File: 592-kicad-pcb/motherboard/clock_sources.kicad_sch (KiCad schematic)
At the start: 28 parts, among them J6 U.FL, U5 SMXS-04K, U6 SX3M10.000B10F20TNN, U7 74LVC1T45GW, U8 SN74LVC1G3157DBVR, U9 SN74LVC1G3157DBVR, Y1 NX3225GA-25.000M-STD-CRG-2, Y2 Si5351A

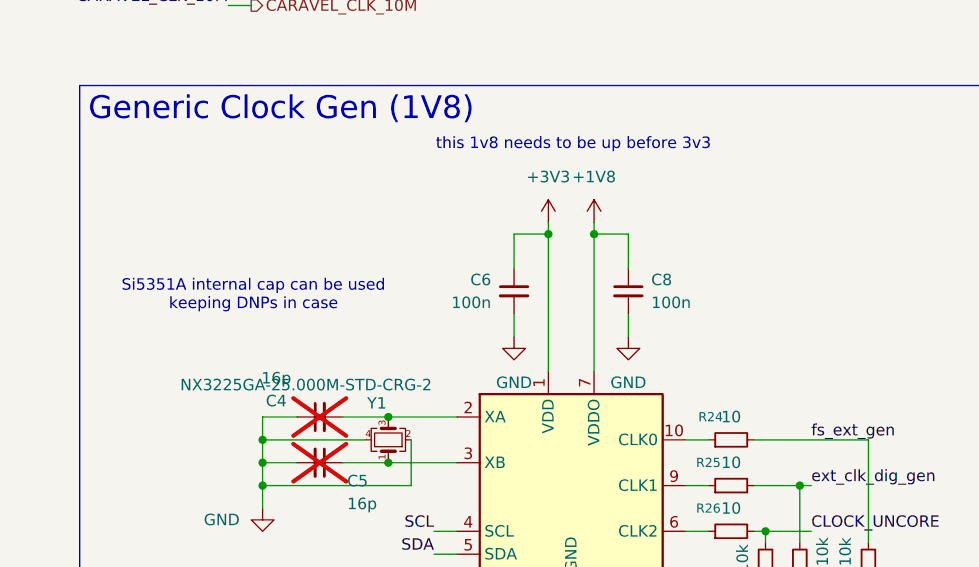
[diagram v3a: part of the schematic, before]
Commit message: add JLC part num for parts, footprints
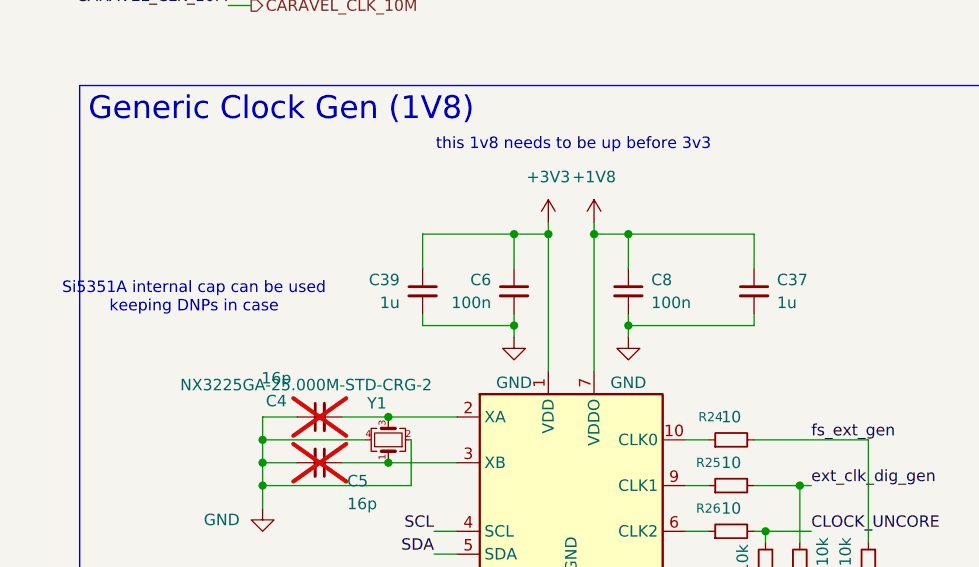
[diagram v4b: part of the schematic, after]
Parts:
- added C37, C39: 1u, Capacitor_SMD:C_0603_1608Metric, symbol Device:C_Small
- C10, C6, C7, C8, C9: footprint Capacitor_SMD:C_0603_1608Metric -> Capacitor_SMD:C_0402_1005Metric; LCSC (none) -> C1525
- C11: footprint Capacitor_SMD:C_0603_1608Metric -> Capacitor_SMD:C_0402_1005Metric; LCSC (none) -> C15195
- C4, C5: footprint Capacitor_SMD:C_0603_1608Metric -> Capacitor_SMD:C_0402_1005Metric
- J6: LCSC (none) -> C5137195
- R22, R23, R27, R28, R29, R30, R31, R32, R33: footprint Resistor_SMD:R_0603_1608Metric -> Resistor_SMD:R_0402_1005Metric; LCSC (none) -> C25744
- R24, R25, R26: footprint Resistor_SMD:R_0603_1608Metric -> Resistor_SMD:R_0402_1005Metric; LCSC (none) -> C25077
- U5: LCSC (none) -> C5439763
- U6: footprint (none) -> Crystal:Crystal_SMD_3225-4Pin_3.2x2.5mm; LCSC (none) -> C5452682
- U7: LCSC (none) -> C478004
- U8, U9: LCSC (none) -> C10426
- Y1: LCSC (none) -> C1985619
- Y2: LCSC (none) -> C504891
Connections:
- net +1V8: now also C37.1
- net +3V3: now also C39.1
- net GND: now also C37.2, C39.2

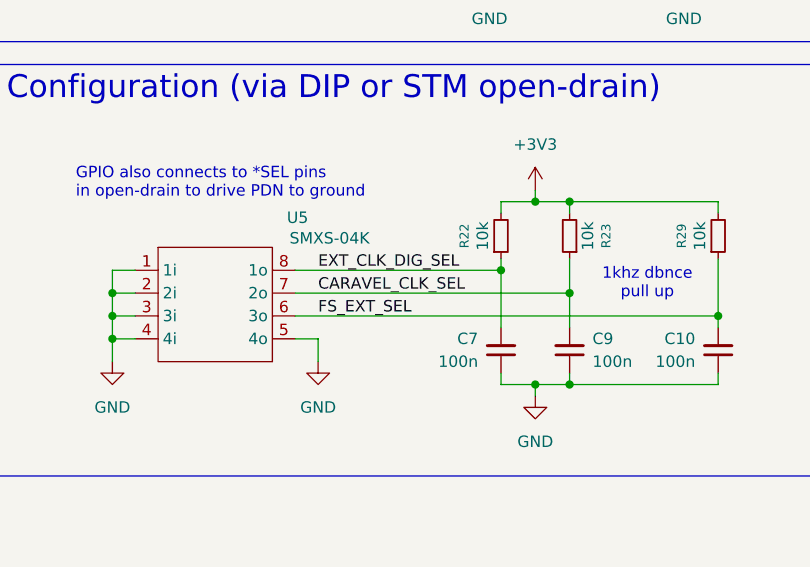
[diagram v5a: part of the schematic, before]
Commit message: update motherboard floorplanning
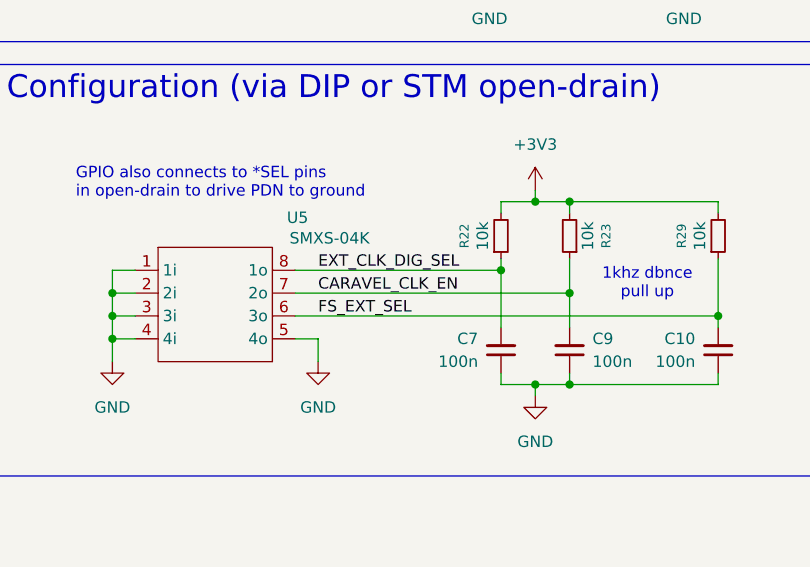
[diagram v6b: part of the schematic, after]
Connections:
- net CARAVEL_CLK_SEL is gone; now on net CARAVEL_CLK_EN: C9.2, R23.1, U5.7 (2o)
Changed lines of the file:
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@@
 		)
 	)
-	(label "CARAVEL_CLK_SEL"
+	(label "CARAVEL_CLK_EN"
 		(at 62.23 157.48 0)
 		(effects

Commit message: updates to routing
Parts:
- renumbered C9 to C10, C37 to C11, C10 to C12, C11 to C13, C39 to C6, C6 to C7, C7 to C8, C8 to C9, J6 to J9, R22 to R23, R23 to R24, R24 to R25, R25 to R26, R26 to R27, R27 to R28, R28 to R29, R29 to R30, R30 to R31, R31 to R32, R32 to R33, R33 to R34, U9 to U10, U5 to U6, U6 to U7, U7 to U8, U8 to U9
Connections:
- net ext_clk_dig_gen: now also R25.2, R31.2; no longer R26.2, R29.2
- net fs_ext_gen: now also R26.2, R29.2; no longer R25.2, R31.2

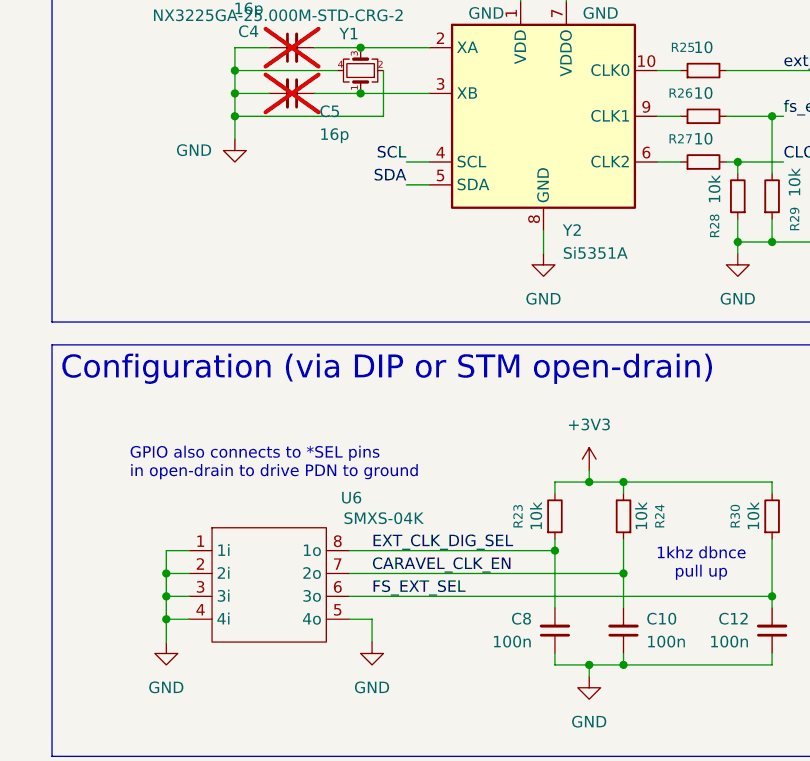
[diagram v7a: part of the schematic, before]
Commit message: more routing progress, add termination resistors
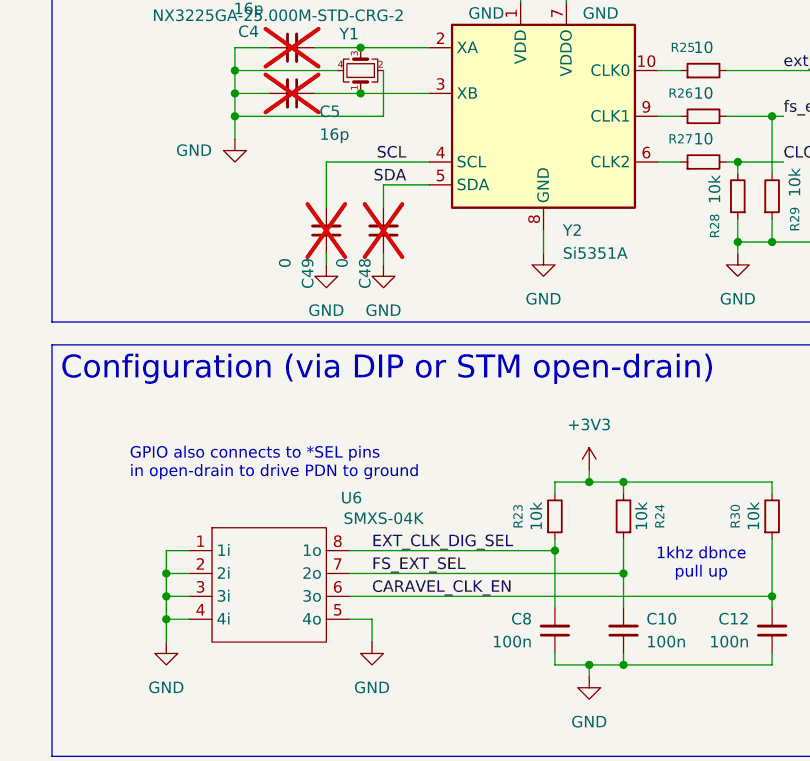
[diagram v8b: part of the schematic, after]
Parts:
- added C48, C49: 0, Capacitor_SMD:C_0402_1005Metric, symbol Device:C_Small
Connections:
- net CARAVEL_CLK_EN: now also C12.2, R30.1, U6.6 (3o); no longer C10.2, R24.1, U6.7 (2o)
- net FS_EXT_SEL: now also C10.2, R24.1, U6.7 (2o); no longer C12.2, R30.1, U6.6 (3o)
- net GND: now also C48.1, C49.1
- net SCL: now also C49.2
- net SDA: now also C48.2
